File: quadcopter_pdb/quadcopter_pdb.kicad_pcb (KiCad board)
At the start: 2 copper layers, 147.4 x 114.5 mm, 38 parts, among them P1 XT60_SMT, P10 CONN_01X03, P11 CONN_01X03, P12 CONN_01X03, P13 CONN_02X25, P14 CONN_02X25, P2 XT60_SMT, P3 XT60_SMT, P4 CONN_01X07, P5 CONN_01X02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

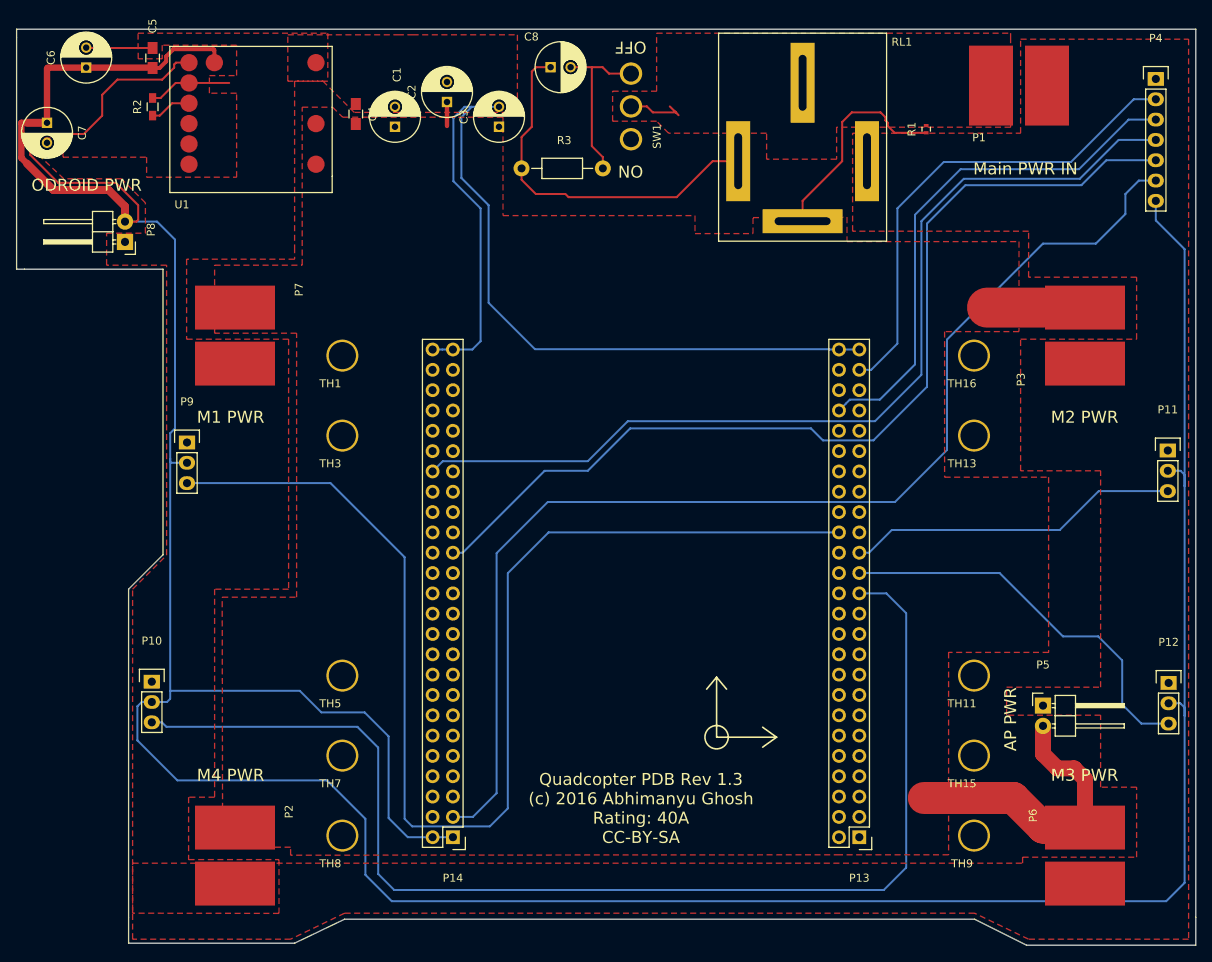
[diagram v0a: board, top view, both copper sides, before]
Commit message: Updating silkscreen on Quadcopter PDB.
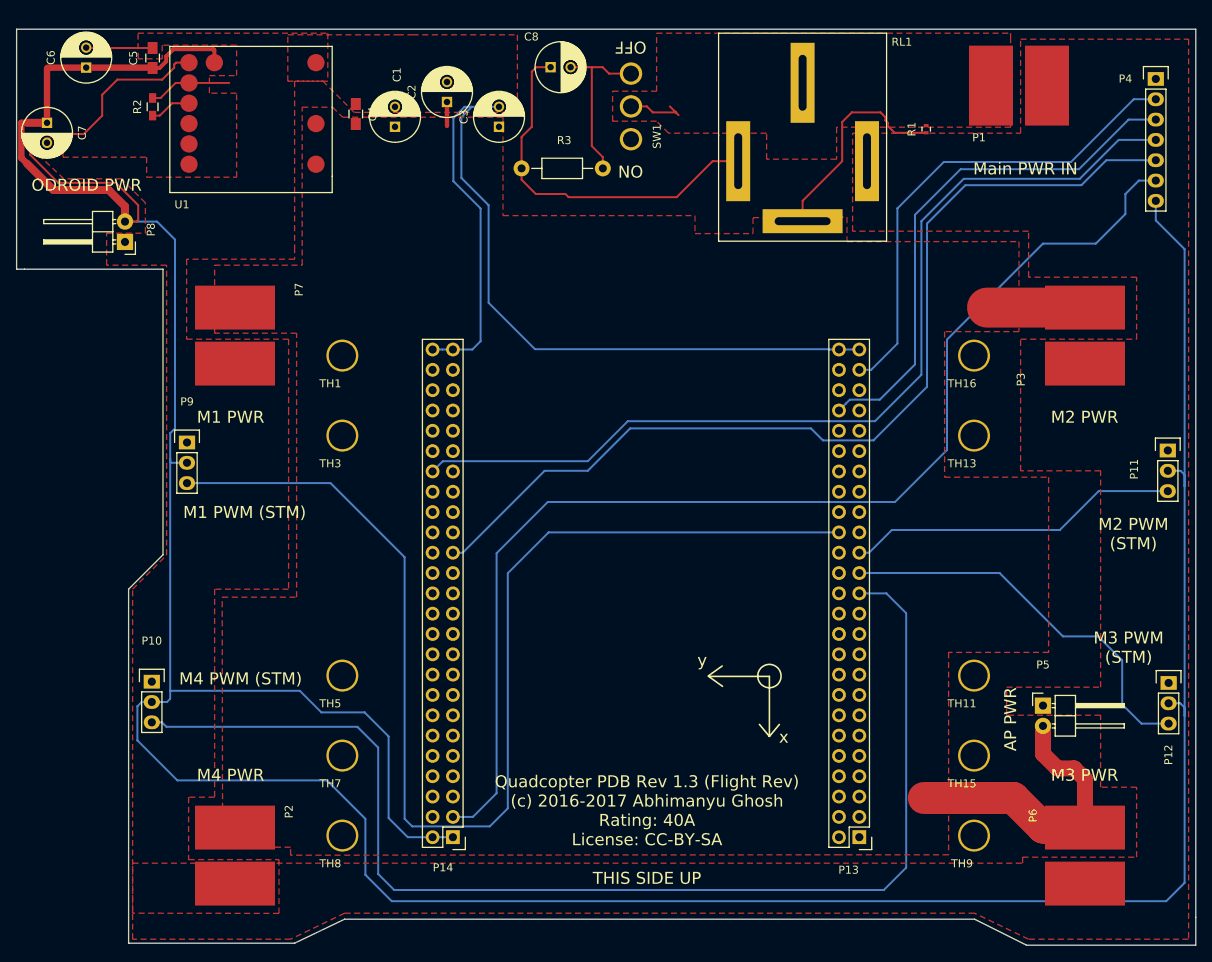
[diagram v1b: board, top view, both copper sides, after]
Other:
- board text added: "M1 PWM (STM)"
- board text added: "M2 PWM (STM)"
- board text added: "M3 PWM (STM)"
- board text added: "M4 PWM (STM)"
- board text added: "Quadcopter PDB Rev 1.3 (Flight Rev) (c) 2016-2017 Abhimanyu Ghosh Rating: 40A License: CC-BY-SA THIS SIDE UP"
- board text added: "x"
- board text added: "y"
- board text removed: "Quadcopter PDB Rev 1.3 (c) 2016 Abhimanyu Ghosh Rating: 40A CC-BY-SA"
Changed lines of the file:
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@@
     (links 66)
     (no_connects 0)
-    (area 73.425 37.423809 224.033334 153.575001)
+    (area 74.924999 38.924999 222.475001 153.575001)
     (thickness 1.6)
-    (drawings 33)
+    (drawings 39)
     (tracks 245)
     (zones 0)
@@
     (visible_elements FFFFFF7F)
     (pcbplotparams
-      (layerselection 0x010f0_80000001)
+      (layerselection 0x010fc_80000001)
       (usegerberextensions false)
       (excludeedgelayer true)
@@
     (tags "capacitor 0805")
     (attr smd)
-    (fp_text reference C5 (at -4 0 270) (layer F.SilkS)
+    (fp_text reference C5 (at 0 2.4 270) (layer F.SilkS)
       (effects (font (size 1 1) (thickness 0.15)))
     )
@@
     (descr "Through hole pin header")
     (tags "pin header")
-    (fp_text reference P11 (at 0 -5.1) (layer F.SilkS)
+    (fp_text reference P11 (at -4.2 2.34 90) (layer F.SilkS)
       (effects (font (size 1 1) (thickness 0.15)))
     )
@@
     (descr "Through hole pin header")
     (tags "pin header")
-    (fp_text reference P12 (at 0 -5.1) (layer F.SilkS)
+    (fp_text reference P12 (at 0 8.98 90) (layer F.SilkS)
       (effects (font (size 1 1) (thickness 0.15)))
     )
@@
     (descr "Through hole pin header")
     (tags "pin header")
-    (fp_text reference P13 (at 0 -5.1 180) (layer F.SilkS)
+    (fp_text reference P13 (at 1.34 -4.1 180) (layer F.SilkS)
       (effects (font (size 1 1) (thickness 0.15)))
     )
@@
     (descr "Through hole pin header")
     (tags "pin header")
-    (fp_text reference P14 (at 0 -5.1 180) (layer F.SilkS)
+    (fp_text reference P14 (at 1.24 -3.8 180) (layer F.SilkS)
       (effects (font (size 1 1) (thickness 0.15)))
     )
@@
     (descr "Through hole pin header")
     (tags "pin header")
-    (fp_text reference P4 (at 0 -5.1) (layer F.SilkS)
+    (fp_text reference P4 (at -3.8 -0.02) (layer F.SilkS)
       (effects (font (size 1 1) (thickness 0.15)))
     )
@@
     )
   )
+  (gr_text "M2 PWM\n(STM)" (at 214.6 102.1) (layer F.SilkS)
+    (effects (font (size 1.5 1.5) (thickness 0.3)))
+  )
+  (gr_text "M3 PWM\n(STM)" (at 214 116.3) (layer F.SilkS)
+    (effects (font (size 1.5 1.5) (thickness 0.3)))
+  )
+  (gr_text "M4 PWM (STM)" (at 103 120.2) (layer F.SilkS)
+    (effects (font (size 1.5 1.5) (thickness 0.3)))
+  )
+  (gr_text "M1 PWM (STM)" (at 103.5 99.4) (layer F.SilkS)
+    (effects (font (size 1.5 1.5) (thickness 0.3)))
+  )
+  (gr_text y (at 160.7 117.9) (layer F.SilkS)
+    (effects (font (size 1.5 1.5) (thickness 0.3)))
+  )
+  (gr_text x (at 170.9 127.5) (layer F.SilkS)
+    (effects (font (size 1.5 1.5) (thickness 0.3)))
+  )
   (gr_text "AP PWR" (at 199.25 125.25 90) (layer F.SilkS)
     (effects (font (size 1.5 1.5) (thickness 0.3)))
@@
     (effects (font (size 1.5 1.5) (thickness 0.3)))
   )
-  (gr_circle (center 162.5 127.5) (end 163.75 126.75) (layer F.SilkS) (width 0.2))
-  (gr_line (start 170 127.5) (end 168.25 128.75) (layer F.SilkS) (width 0.2))
-  (gr_line (start 170 127.5) (end 168.25 126.25) (layer F.SilkS) (width 0.2))
-  (gr_line (start 162.5 127.5) (end 170 127.5) (layer F.SilkS) (width 0.2))
-  (gr_line (start 162.5 120) (end 163.75 121.5) (layer F.SilkS) (width 0.2))
-  (gr_line (start 162.5 120) (end 161.25 121.5) (layer F.SilkS) (width 0.2))
-  (gr_line (start 162.5 127.5) (end 162.5 120) (layer F.SilkS) (width 0.2))
+  (gr_circle (center 169.1 119.857737) (end 170.35 119.107737) (layer F.SilkS) (width 0.2))
+  (gr_line (start 163.2 118.6) (end 161.45 119.85) (layer F.SilkS) (width 0.2))
+  (gr_line (start 163.25 121.15) (end 161.5 119.9) (layer F.SilkS) (width 0.2))
+  (gr_line (start 161.6 119.9) (end 169.1 119.9) (layer F.SilkS) (width 0.2))
+  (gr_line (start 167.85 125.9) (end 169.1 127.4) (layer F.SilkS) (width 0.2))
+  (gr_line (start 170.35 125.9) (end 169.1 127.4) (layer F.SilkS) (width 0.2))
+  (gr_line (start 169.1 127.4) (end 169.1 119.9) (layer F.SilkS) (width 0.2))
   (gr_text OFF (at 151.75 41.25 180) (layer F.SilkS)
     (effects (font (size 1.5 1.5) (thickness 0.3)))
@@
     (effects (font (size 1.5 1.5) (thickness 0.3)))
   )
-  (gr_text "Quadcopter PDB Rev 1.3\n(c) 2016 Abhimanyu Ghosh\nRating: 40A\nCC-BY-SA" (at 153.05 136.4) (layer F.SilkS)
-    (effects (font (size 1.5 1.5) (thickness 0.3)))
-  )
+  (gr_text "Quadcopter PDB Rev 1.3 (Flight Rev)\n(c) 2016-2017 Abhimanyu Ghosh\nRating: 40A\nLicense: CC-BY-SA\n\nTHIS SIDE UP" (at 153.8 139.1) (layer F.SilkS)
+    (effects (font (size 1.5 1.5) (thickness 0.3)))
+  )

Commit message: Updating Quadcopter PDB to latest combined design capable of accomodating AP or STM32 systems.
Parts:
- added P15: CONN_02X20, Pin_Headers:Pin_Header_Straight_2x20, F.Cu at (170.0, 79.8)
- added P16: CONN_01X04, Pin_Headers:Pin_Header_Straight_1x04, F.Cu at (163.5, 144.4)
- added P17: CONN_01X04, Pin_Headers:Pin_Header_Straight_1x04, F.Cu at (98.4, 111.7)
- added P18: CONN_01X04, Pin_Headers:Pin_Header_Straight_1x04, F.Cu at (213.6, 106.7)
- added P19: CONN_01X04, Pin_Headers:Pin_Header_Straight_1x04, F.Cu at (147.0, 144.5)
- moved P11 2.60 mm to (216.3, 91.7)
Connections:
- P10 pad 2: /ODROID_5V -> (no net)
- P11 pad 2: /ODROID_5V -> (no net)
- P12 pad 2: /ODROID_5V -> (no net)
- P13 pad 11: (no net) -> /UART2_RX
- P13 pad 14: (no net) -> /UART2_TX
- P13 pad 33: (no net) -> /UART3_RX
- P13 pad 34: (no net) -> /UART3_TX
- P14 pad 21: (no net) -> /I2C1_SCL
- P14 pad 22: (no net) -> /I2C1_SDA
- P9 pad 2: /ODROID_5V -> (no net)
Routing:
- net /ODROID_5V: track 466.1 -> 52.0 mm, vias 0 -> 5
- net Earth: track 136.3 -> 34.1 mm, vias 0 -> 4
- net /UART3_TX: track 0.00 -> 79.9 mm
- net /UART3_RX: track 0.00 -> 74.2 mm
- net /PI_TX: track 0.00 -> 64.6 mm, vias 0 -> 1
- net /PI_RX: track 0.00 -> 64.1 mm, vias 0 -> 1
- net /M4_PWM: track 155.1 -> 95.7 mm, vias 0 -> 2
- net /M1_PWM: track 150.9 -> 92.2 mm, vias 0 -> 2
- net /UART2_TX: track 0.00 -> 53.7 mm
- net /UART2_RX: track 0.00 -> 49.8 mm
- net /I2C1_SCL: track 0.00 -> 36.0 mm
- net /I2C1_SDA: track 0.00 -> 33.0 mm
- net /RC_5: track 147.9 -> 169.6 mm, vias 0 -> 1
- net /RC_4: track 121.4 -> 135.4 mm, vias 0 -> 1
- net /RC_3: track 118.8 -> 127.0 mm, vias 0 -> 1
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- added copper zone on B.Cu, net /ODROID_5V
- added copper zone on F.Cu, net /ODROID_5V
- added copper zone on B.Cu, net Earth
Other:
- outline, holes or cut-outs redrawn
- board text added: "5V"
- board text added: "AUX/NMEA"
- board text added: "GND"
- board text added: "GND RX TX 5V"
- board text added: "LIDAR"
- board text added: "PI DEBUG"
- board text added: "PXFLOW"
- board text added: "Quadcopter PDB Rev 1.3 (Flight Rev) (c) 2016-2017 Abhimanyu Ghosh Rating: 40A License: CC-BY-SA"
- board text added: "RC PWM IN"
- board text added: "SCL"
- board text added: "SDA"
- board text added: "THIS SIDE UP"
- board text removed: "Quadcopter PDB Rev 1.3 (Flight Rev) (c) 2016-2017 Abhimanyu Ghosh Rating: 40A License: CC-BY-SA THIS SIDE UP"

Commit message: One last update.
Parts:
- added ?: Symbol_OSHW-Logo_SilkScreen, Symbols:Symbol_OSHW-Logo_SilkScreen, F.Cu at (144.0, 121.0)
- added TH10: PTH, Mounting_Holes:MountingHole_3mm, F.Cu at (122.3, 74.8)
- added TH2: PTH, Mounting_Holes:MountingHole_3mm, F.Cu at (171.3, 74.8)
- added TH4: PTH, Mounting_Holes:MountingHole_3mm, F.Cu at (171.3, 132.8)
- added TH6: PTH, Mounting_Holes:MountingHole_3mm, F.Cu at (122.3, 132.8)
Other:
- board text added: "Quadcopter PDB Rev 1.3 Flight Rev (c) 2016-2017 Abhimanyu Ghosh Rating: 40A License: CC-BY-SA"
- board text removed: "Quadcopter PDB Rev 1.3 (Flight Rev) (c) 2016-2017 Abhimanyu Ghosh Rating: 40A License: CC-BY-SA"
